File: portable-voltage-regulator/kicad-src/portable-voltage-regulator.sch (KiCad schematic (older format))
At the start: 13 parts, among them J1 Conn_01x03, Q1 IRF9540N, U1 ADR293GRUZ, U2 OPA333xxD

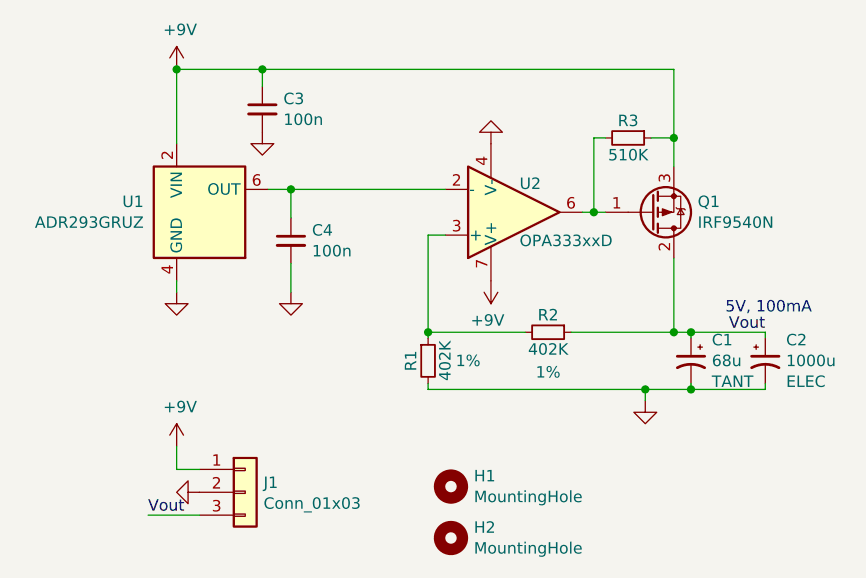
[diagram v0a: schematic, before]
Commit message: upgrade opamp
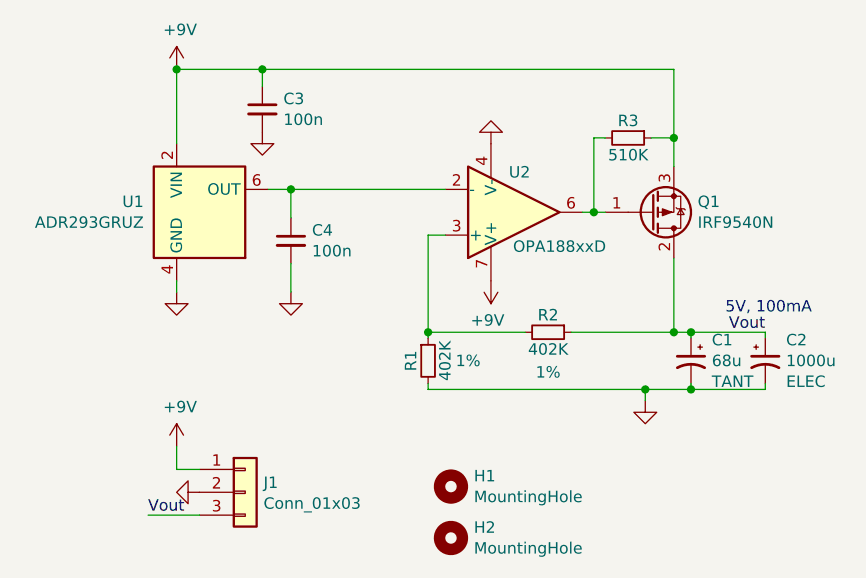
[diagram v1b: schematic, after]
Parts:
- removed U2: OPA333xxD, Package_SO:SOIC-8_3.9x4.9mm_P1.27mm, symbol Amplifier_Operational:OPA333xxD
- added U2: OPA188xxD, Package_SO:SOIC-8_3.9x4.9mm_P1.27mm, symbol Amplifier_Operational:OPA188xxD
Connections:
- net +9V: now also U2.7 (V+)
- net GND: now also U2.4 (V-)
- net at Q1.1 (G), R3.2: now also U2.6
- net at C4.1, U1.6 (OUT): now also U2.2 (-)
- net at R1.1, R2.2: now also U2.3 (+)
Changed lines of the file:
@@
 	4500 4175 4500 4225
-$Comp
-L Amplifier_Operational:OPA333xxD U2
-U 1 1 61C3F360
-P 5975 3875
-F 0 "U2" H 6000 3750 50  0000 L CNN
-F 1 "OPA333xxD" H 6000 4000 50  0000 L CNN
-F 2 "Package_SO:SOIC-8_3.9x4.9mm_P1.27mm" H 5875 3675 50  0001 L CNN
-F 3 "http://www.ti.com/lit/ds/symlink/opa333.pdf" H 6125 4025 50  0001 C CNN
-	1    5975 3875
-	1    0    0    1
-$EndComp
 $Comp
 L power:+9V #PWR01
@@
 	1    0    0    -1
 $EndComp
+$Comp
+L Amplifier_Operational:OPA188xxD U2
+U 1 1 61C34A1C
+P 5975 3875
+F 0 "U2" H 6000 3700 50  0000 C CNN
+F 1 "OPA188xxD" H 6175 4025 50  0000 C CNN
+F 2 "Package_SO:SOIC-8_3.9x4.9mm_P1.27mm" H 5875 3675 50  0001 L CNN
+F 3 "http://www.ti.com/lit/ds/symlink/opa188.pdf" H 6125 4025 50  0001 C CNN
+	1    5975 3875
+	1    0    0    1
+$EndComp
 $EndSCHEMATC
